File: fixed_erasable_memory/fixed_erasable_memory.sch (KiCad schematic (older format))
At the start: 1 part, among them P1 DIN_41612_128P

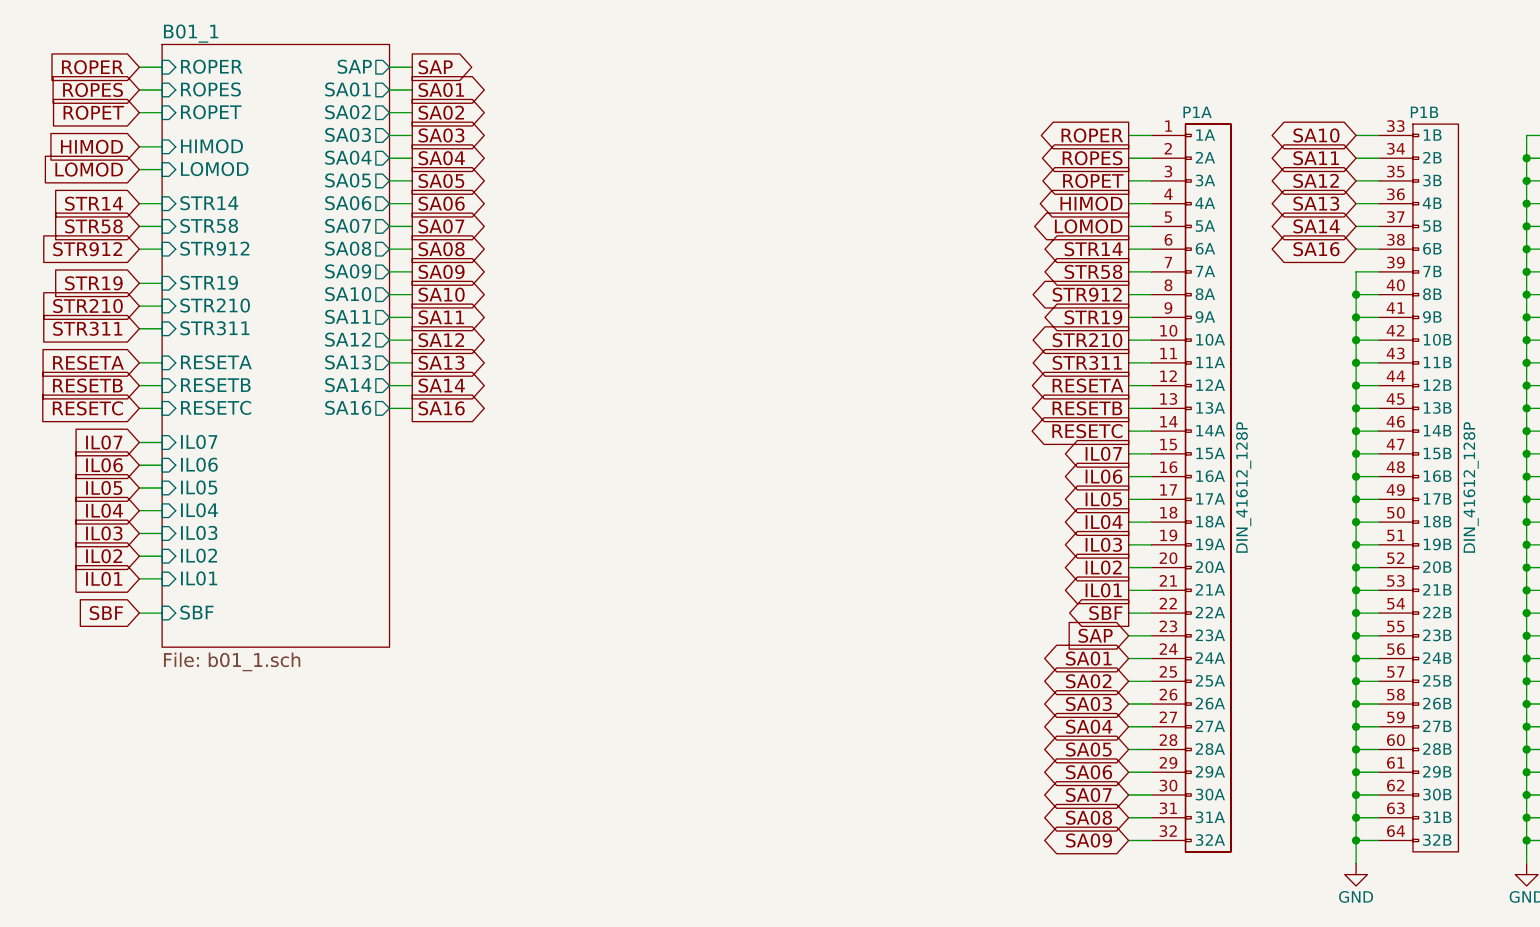
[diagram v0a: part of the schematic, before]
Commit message: Updated fixed memory model, plus various bugfixes
Rope memory control signals are now decoded much earlier in the cycle to
determine the target address, allowing slower memory devices (such as
the EPCS on the DE0 Nano) enough time to load their data.

The bugfixes are mostly wiring errors discovered by debugging lockups in
when running Colossus 237 -- all were causing the ST2 pulse to not
occur, so errors that *don't* prevent ST2 from happening very well might
be present in the instructions that have been fixed.

The computer now gets through the initialization code and enters an
infinite loop when attempting to invoke the interpeter, due to the lack
of erasable memory.
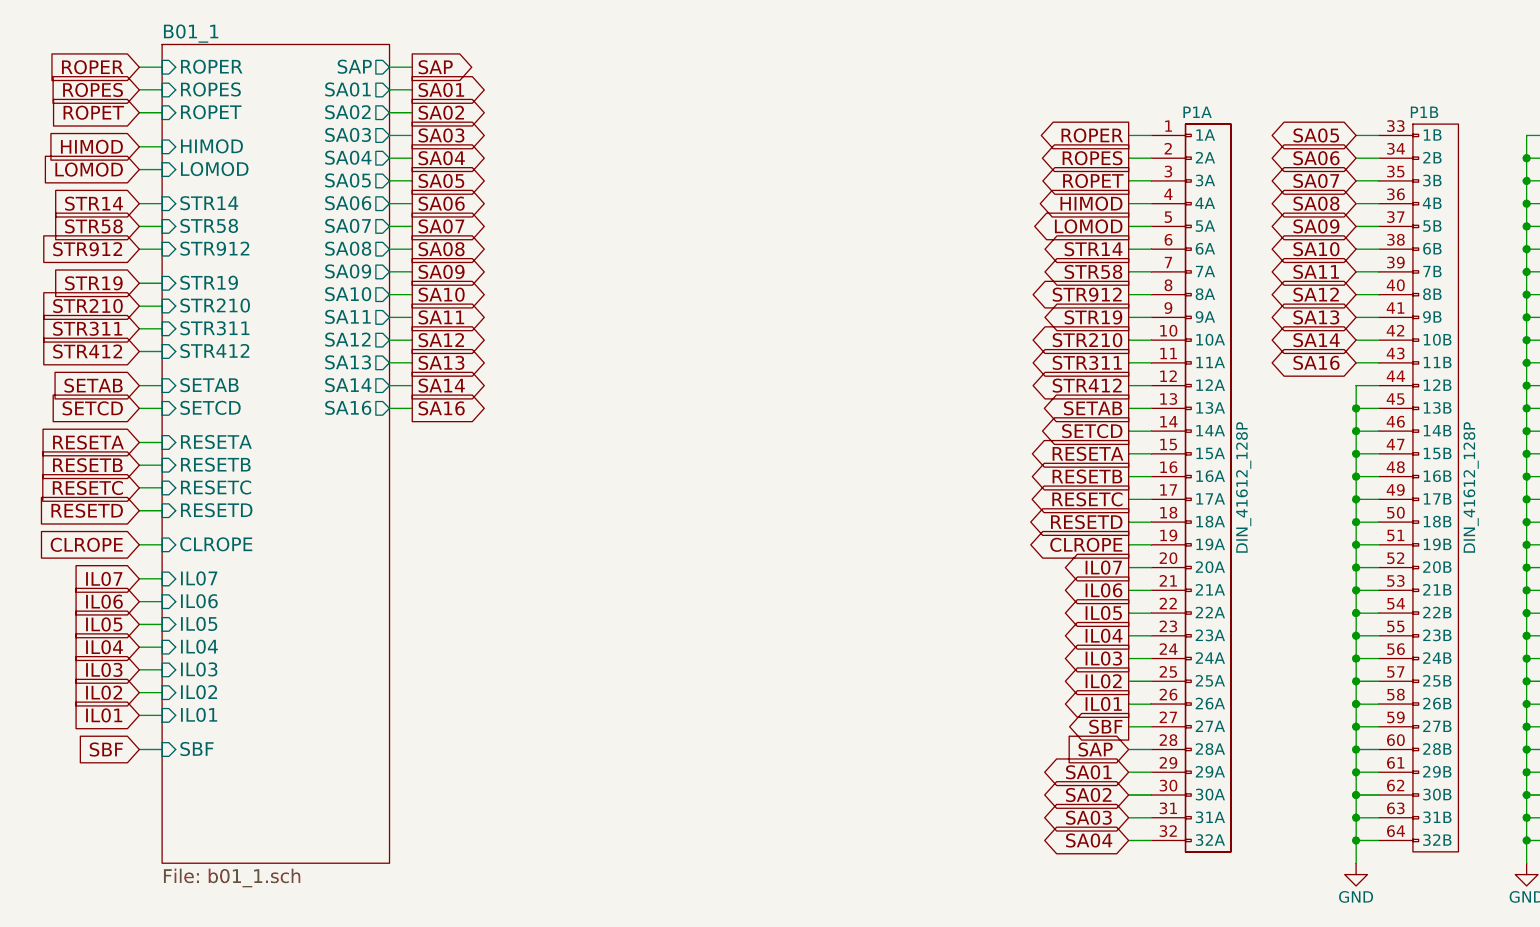
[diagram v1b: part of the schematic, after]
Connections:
- net GND: no longer P1.39 (7B), P1.40 (8B), P1.41 (9B), P1.42 (10B), P1.43 (11B)
- net IL01: now also P1.26 (26A); no longer P1.21 (21A)
- net IL02: now also P1.25 (25A); no longer P1.20 (20A)
- net IL03: now also P1.24 (24A); no longer P1.19 (19A)
- net IL04: now also P1.23 (23A); no longer P1.18 (18A)
- net IL05: now also P1.22 (22A); no longer P1.17 (17A)
- net IL06: now also P1.21 (21A); no longer P1.16 (16A)
- net IL07: now also P1.20 (20A); no longer P1.15 (15A)
- net RESETA: now also P1.15 (15A); no longer P1.12 (12A)
- net RESETB: now also P1.16 (16A); no longer P1.13 (13A)
- net RESETC: now also P1.17 (17A); no longer P1.14 (14A)
- net SA01: now also P1.29 (29A); no longer P1.24 (24A)
- net SA02: now also P1.30 (30A); no longer P1.25 (25A)
- net SA03: now also P1.31 (31A); no longer P1.26 (26A)
- net SA04: now also P1.32 (32A); no longer P1.27 (27A)
- net SA05: now also P1.33 (1B); no longer P1.28 (28A)
- net SA06: now also P1.34 (2B); no longer P1.29 (29A)
- net SA07: now also P1.35 (3B); no longer P1.30 (30A)
- net SA08: now also P1.36 (4B); no longer P1.31 (31A)
- net SA09: now also P1.37 (5B); no longer P1.32 (32A)
- net SA10: now also P1.38 (6B); no longer P1.33 (1B)
- net SA11: now also P1.39 (7B); no longer P1.34 (2B)
- net SA12: now also P1.40 (8B); no longer P1.35 (3B)
- net SA13: now also P1.41 (9B); no longer P1.36 (4B)
- net SA14: now also P1.42 (10B); no longer P1.37 (5B)
- net SA16: now also P1.43 (11B); no longer P1.38 (6B)
- net SAP: now also P1.28 (28A); no longer P1.23 (23A)
- net SBF: now also P1.27 (27A); no longer P1.22 (22A)
- new net CLROPE: P1.19 (19A)
- new net RESETD: P1.18 (18A)
- new net SETAB: P1.13 (13A)
- new net SETCD: P1.14 (14A)
- new net STR412: P1.12 (12A)
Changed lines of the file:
@@
 $EndComp
-Wire Wire Line
-	7500 2700 7600 2700
-Connection ~ 7500 2700
-Wire Wire Line
-	7500 2800 7600 2800
-Connection ~ 7500 2800
-Wire Wire Line
-	7500 2900 7600 2900
-Connection ~ 7500 2900
 Wire Wire Line
 	7500 3000 7600 3000
-Connection ~ 7500 3000
 Wire Wire Line
 	7500 3100 7600 3100
@@
 $EndComp
 $Sheet
-S 2250 1500 1000 2650
+S 2250 1500 1000 3600
 U 56CD3779
 F0 "B01_1" 60
@@
 F16 "SA09" O R 3250 2500 60
 F17 "SA08" O R 3250 2400 60
-F18 "SBF" I L 2250 4000 60
+F18 "SBF" I L 2250 4600 60
 F19 "ROPER" I L 2250 1600 60
 F20 "ROPES" I L 2250 1700 60
@@
 F28 "STR19" I L 2250 2550 60
 F29 "STR311" I L 2250 2750 60
-F30 "RESETB" I L 2250 3000 60
-F31 "RESETA" I L 2250 2900 60
-F32 "RESETC" I L 2250 3100 60
-F33 "IL07" I L 2250 3250 60
-F34 "IL06" I L 2250 3350 60
-F35 "IL05" I L 2250 3450 60
-F36 "IL04" I L 2250 3550 60
-F37 "IL03" I L 2250 3650 60
-F38 "IL02" I L 2250 3750 60
-F39 "IL01" I L 2250 3850 60
+F30 "RESETB" I L 2250 3350 60
+F31 "RESETA" I L 2250 3250 60
+F32 "RESETC" I L 2250 3450 60
+F33 "IL07" I L 2250 3850 60
+F34 "IL06" I L 2250 3950 60
+F35 "IL05" I L 2250 4050 60
+F36 "IL04" I L 2250 4150 60
+F37 "IL03" I L 2250 4250 60
+F38 "IL02" I L 2250 4350 60
+F39 "IL01" I L 2250 4450 60
+F40 "STR412" I L 2250 2850 60
+F41 "SETAB" I L 2250 3000 60
+F42 "SETCD" I L 2250 3100 60
+F43 "RESETD" I L 2250 3550 60
+F44 "CLROPE" I L 2250 3700 60
 $EndSheet
 Text GLabel 2150 1600 0    60   Input ~ 0
@@
 Wire Wire Line
 	2150 2750 2250 2750
-Text GLabel 2150 2900 0    60   Input ~ 0
+Text GLabel 2150 3250 0    60   Input ~ 0
 RESETA
-Wire Wire Line
-	2150 2900 2250 2900
-Text GLabel 2150 3000 0    60   Input ~ 0
-RESETB
-Wire Wire Line
-	2150 3000 2250 3000
-Text GLabel 2150 3100 0    60   Input ~ 0
-RESETC
-Wire Wire Line
-	2150 3100 2250 3100
-Text GLabel 2150 3250 0    60   Input ~ 0
-IL07
 Wire Wire Line
 	2150 3250 2250 3250
 Text GLabel 2150 3350 0    60   Input ~ 0
-IL06
+RESETB
 Wire Wire Line
 	2150 3350 2250 3350
 Text GLabel 2150 3450 0    60   Input ~ 0
+RESETC
+Wire Wire Line
+	2150 3450 2250 3450
+Text GLabel 2150 3850 0    60   Input ~ 0
+IL07
+Wire Wire Line
+	2150 3850 2250 3850
+Text GLabel 2150 3950 0    60   Input ~ 0
+IL06
+Wire Wire Line
+	2150 3950 2250 3950
+Text GLabel 2150 4050 0    60   Input ~ 0
 IL05
 Wire Wire Line
-	2150 3450 2250 3450
-Text GLabel 2150 3550 0    60   Input ~ 0
+	2150 4050 2250 4050
+Text GLabel 2150 4150 0    60   Input ~ 0
 IL04
 Wire Wire Line
-	2150 3550 2250 3550
-Text GLabel 2150 3650 0    60   Input ~ 0
+	2150 4150 2250 4150
+Text GLabel 2150 4250 0    60   Input ~ 0
 IL03
 Wire Wire Line
-	2150 3650 2250 3650
-Text GLabel 2150 3750 0    60   Input ~ 0
+	2150 4250 2250 4250
+Text GLabel 2150 4350 0    60   Input ~ 0
 IL02
 Wire Wire Line
-	2150 3750 2250 3750
-Text GLabel 2150 3850 0    60   Input ~ 0
+	2150 4350 2250 4350
+Text GLabel 2150 4450 0    60   Input ~ 0
 IL01
 Wire Wire Line
-	2150 3850 2250 3850
-Text GLabel 2150 4000 0    60   Input ~ 0
+	2150 4450 2250 4450
+Text GLabel 2150 4600 0    60   Input ~ 0
 SBF
 Wire Wire Line
-	2150 4000 2250 4000
+	2150 4600 2250 4600
 Text GLabel 6500 1900 0    60   Output ~ 0
 ROPER
@@
 Wire Wire Line
 	6500 2900 6600 2900
-Text GLabel 6500 3000 0    60   Output ~ 0
+Text GLabel 6500 3300 0    60   Output ~ 0
 RESETA
-Wire Wire Line
-	6500 3000 6600 3000
-Text GLabel 6500 3100 0    60   Output ~ 0
-RESETB
-Wire Wire Line
-	6500 3100 6600 3100
-Text GLabel 6500 3200 0    60   Output ~ 0
-RESETC
-Wire Wire Line
-	6500 3200 6600 3200
-Text GLabel 6500 3300 0    60   Output ~ 0
-IL07
 Wire Wire Line
 	6500 3300 6600 3300
 Text GLabel 6500 3400 0    60   Output ~ 0
-IL06
+RESETB
 Wire Wire Line
 	6500 3400 6600 3400
 Text GLabel 6500 3500 0    60   Output ~ 0
-IL05
+RESETC
 Wire Wire Line
 	6500 3500 6600 3500
-Text GLabel 6500 3600 0    60   Output ~ 0
-IL04
-Wire Wire Line
-	6500 3600 6600 3600
-Text GLabel 6500 3700 0    60   Output ~ 0
-IL03
-Wire Wire Line
-	6500 3700 6600 3700
 Text GLabel 6500 3800 0    60   Output ~ 0
-IL02
+IL07
 Wire Wire Line
 	6500 3800 6600 3800
 Text GLabel 6500 3900 0    60   Output ~ 0
-IL01
+IL06
 Wire Wire Line
 	6500 3900 6600 3900
 Text GLabel 6500 4000 0    60   Output ~ 0
+IL05
+Wire Wire Line
+	6500 4000 6600 4000
+Text GLabel 6500 4100 0    60   Output ~ 0
+IL04
+Wire Wire Line
+	6500 4100 6600 4100
+Text GLabel 6500 4200 0    60   Output ~ 0
+IL03
+Wire Wire Line
+	6500 4200 6600 4200
+Text GLabel 6500 4300 0    60   Output ~ 0
+IL02
+Wire Wire Line
+	6500 4300 6600 4300
+Text GLabel 6500 4400 0    60   Output ~ 0
+IL01
+Wire Wire Line
+	6500 4400 6600 4400
+Text GLabel 6500 4500 0    60   Output ~ 0
 SBF
 Wire Wire Line
-	6500 4000 6600 4000
+	6500 4500 6600 4500
 Text GLabel 3350 1600 2    60   Output ~ 0
 SAP
@@
 Wire Wire Line
 	3350 3100 3250 3100
-Text GLabel 6500 4100 0    60   Input ~ 0
+Text GLabel 6500 4600 0    60   Input ~ 0
 SAP
-Wire Wire Line
-	6500 4100 6600 4100
-Text GLabel 6500 4200 0    60   BiDi ~ 0
-SA01
-Wire Wire Line
-	6500 4200 6600 4200
-Text GLabel 6500 4300 0    60   BiDi ~ 0
-SA02
-Wire Wire Line
-	6500 4300 6600 4300
-Text GLabel 6500 4400 0    60   BiDi ~ 0
-SA03
-Wire Wire Line
-	6500 4400 6600 4400
-Text GLabel 6500 4500 0    60   BiDi ~ 0
-SA04
-Wire Wire Line
-	6500 4500 6600 4500
-Text GLabel 6500 4600 0    60   BiDi ~ 0
-SA05
 Wire Wire Line
 	6500 4600 6600 4600
 Text GLabel 6500 4700 0    60   BiDi ~ 0
-SA06
+SA01
 Wire Wire Line
 	6500 4700 6600 4700
 Text GLabel 6500 4800 0    60   BiDi ~ 0
-SA07
+SA02
 Wire Wire Line
 	6500 4800 6600 4800
 Text GLabel 6500 4900 0    60   BiDi ~ 0
-SA08
+SA03
 Wire Wire Line
 	6500 4900 6600 4900
 Text GLabel 6500 5000 0    60   BiDi ~ 0
-SA09
+SA04
 Wire Wire Line
 	6500 5000 6600 5000
 Text GLabel 7500 1900 0    60   BiDi ~ 0
-SA10
+SA05
 Wire Wire Line
 	7500 1900 7600 1900
 Text GLabel 7500 2000 0    60   BiDi ~ 0
-SA11
+SA06
 Wire Wire Line
 	7500 2000 7600 2000
 Text GLabel 7500 2100 0    60   BiDi ~ 0
-SA12
+SA07
 Wire Wire Line
 	7500 2100 7600 2100
 Text GLabel 7500 2200 0    60   BiDi ~ 0
-SA13
+SA08
 Wire Wire Line
 	7500 2200 7600 2200
 Text GLabel 7500 2300 0    60   BiDi ~ 0
-SA14
+SA09
 Wire Wire Line
 	7500 2300 7600 2300
 Text GLabel 7500 2400 0    60   BiDi ~ 0
+SA10
+Wire Wire Line
+	7500 2400 7600 2400
+Text GLabel 7500 2500 0    60   BiDi ~ 0
+SA11
+Wire Wire Line
+	7500 2500 7600 2500
+Text GLabel 7500 2600 0    60   BiDi ~ 0
+SA12
+Wire Wire Line
+	7500 2600 7600 2600
+Text GLabel 7500 2700 0    60   BiDi ~ 0
+SA13
+Wire Wire Line
+	7500 2700 7600 2700
+Text GLabel 7500 2800 0    60   BiDi ~ 0
+SA14
+Wire Wire Line
+	7500 2800 7600 2800
+Text GLabel 7500 2900 0    60   BiDi ~ 0
 SA16
 Wire Wire Line
-	7500 2400 7600 2400
-Wire Wire Line
-	7600 2600 7500 2600
-Connection ~ 7500 2600
-Wire Wire Line
-	7600 2500 7500 2500
-Wire Wire Line
-	7500 2500 7500 5100
+	7500 2900 7600 2900
+Text GLabel 2150 2850 0    60   Input ~ 0
+STR412
+Wire Wire Line
+	2150 2850 2250 2850
+Text GLabel 6500 3000 0    60   Output ~ 0
+STR412
+Wire Wire Line
+	6500 3000 6600 3000
+Text GLabel 2150 3550 0    60   Input ~ 0
+RESETD
+Wire Wire Line
+	2150 3550 2250 3550
+Text GLabel 2150 3000 0    60   Input ~ 0
+SETAB
+Wire Wire Line
+	2150 3000 2250 3000
+Text GLabel 2150 3100 0    60   Input ~ 0
+SETCD
+Wire Wire Line
+	2150 3100 2250 3100
+Text GLabel 6500 3100 0    60   Output ~ 0
+SETAB
+Wire Wire Line
+	6500 3100 6600 3100
+Text GLabel 6500 3200 0    60   Output ~ 0
+SETCD
+Wire Wire Line
+	6500 3200 6600 3200
+Text GLabel 6500 3600 0    60   Output ~ 0
+RESETD
+Wire Wire Line
+	6500 3600 6600 3600
+Text GLabel 2150 3700 0    60   Input ~ 0
+CLROPE
+Wire Wire Line
+	2150 3700 2250 3700
+Wire Wire Line
+	7500 3000 7500 5100
+Text GLabel 6500 3700 0    60   Output ~ 0
+CLROPE
+Wire Wire Line
+	6500 3700 6600 3700
 $EndSCHEMATC
